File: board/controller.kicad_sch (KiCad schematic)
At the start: 0 parts

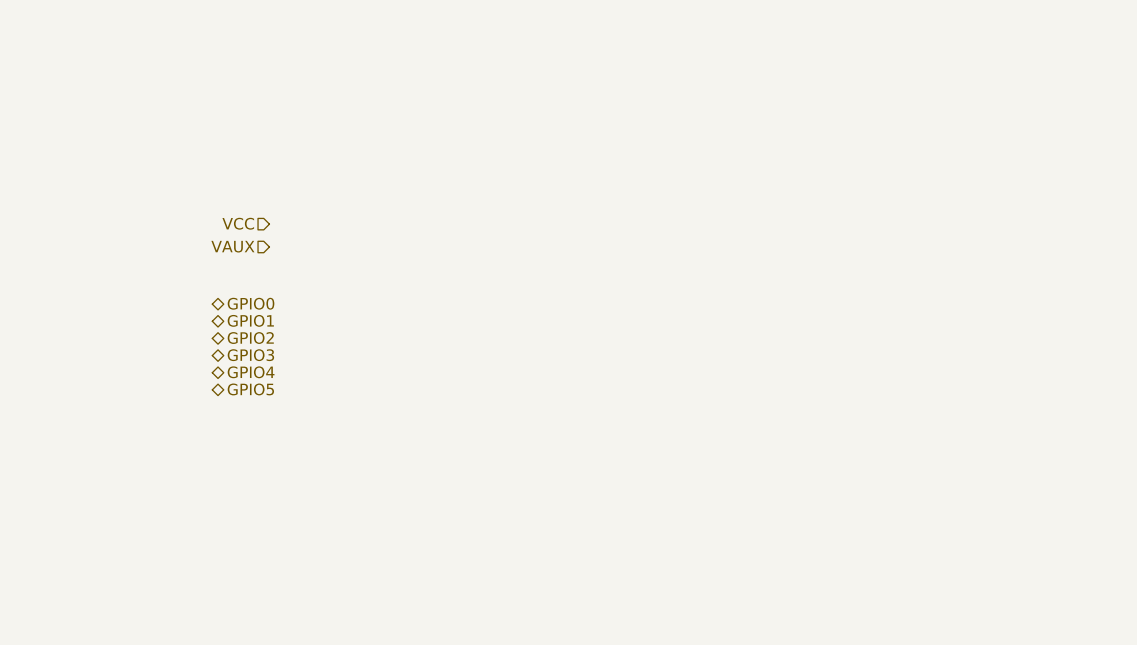
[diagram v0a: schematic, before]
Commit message: Added testpoints and other fixes
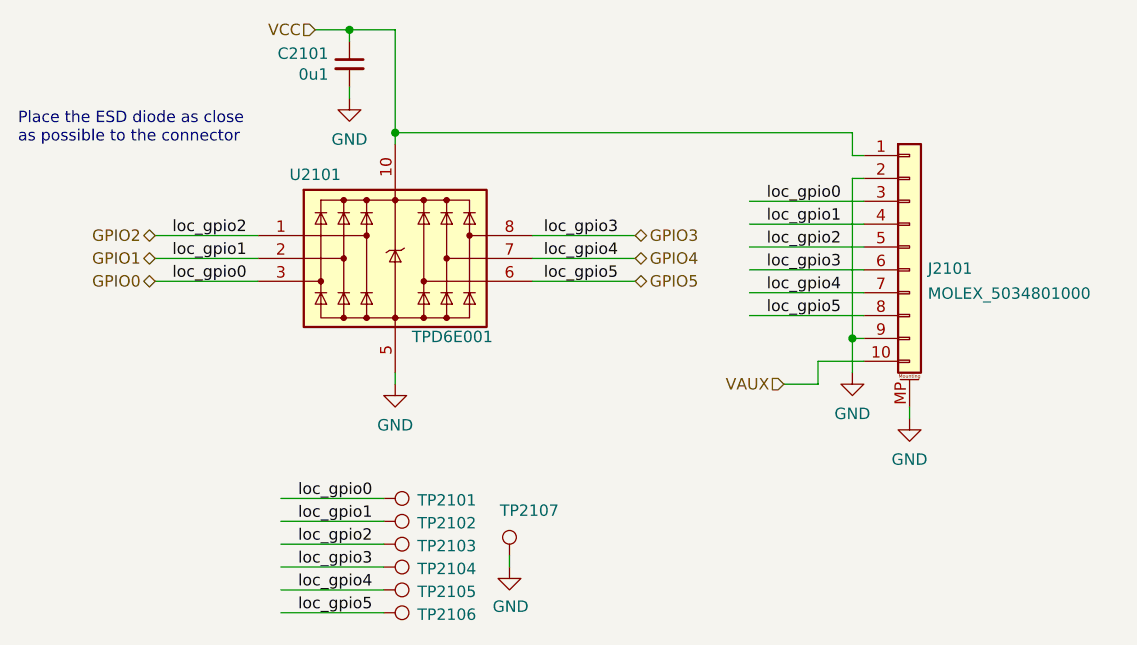
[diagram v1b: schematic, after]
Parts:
- added C2101: 0u1, DIYPie:C_0402_1005Metric, symbol Device:C_Small
- added J2101: MOLEX_5034801000, DIYPie:MOLEX_5034801000, symbol DIYPie:MOLEX_5034801000
- added TP2101, TP2102, TP2103, TP2104, TP2105, TP2106, TP2107: TestPoint, DIYPie:TestPoint_Pad_D1.5mm, symbol DIYPie:TestPoint
- added U2101: TPD6E001, DIYPie:TI_UQFN-10, symbol DIYPie:TPD6E001
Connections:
- net GPIO0: now also J2101.3, TP2101.1, U2101.3
- net GPIO1: now also J2101.4, TP2102.1, U2101.2
- net GPIO2: now also J2101.5, TP2103.1, U2101.1
- net GPIO3: now also J2101.6, TP2104.1, U2101.8
- net GPIO4: now also J2101.7, TP2105.1, U2101.7
- net GPIO5: now also J2101.8, TP2106.1, U2101.6
- net VAUX: now also J2101.10
- net VCC: now also C2101.1, J2101.1, U2101.10
- new net GND: C2101.2, J2101.2, J2101.9, J2101.MP, TP2107.1, U2101.5
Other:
- note added: "Place the ESD diode as close as possible to the connector"
